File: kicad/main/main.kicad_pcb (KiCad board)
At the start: 2 copper layers, 44.5 x 35 mm, 19 parts, among them J2 Conn_01x02, J3 Conn_01x07_Pin, J4 Conn_01x04_Pin, P1 USB_C_Plug_USB2.0, SW1 MK-12C03-G015, SW3 SW_Push, SW4 SW_Push, U1 HUSB237, U2 ZX-PH2.0-WT4P

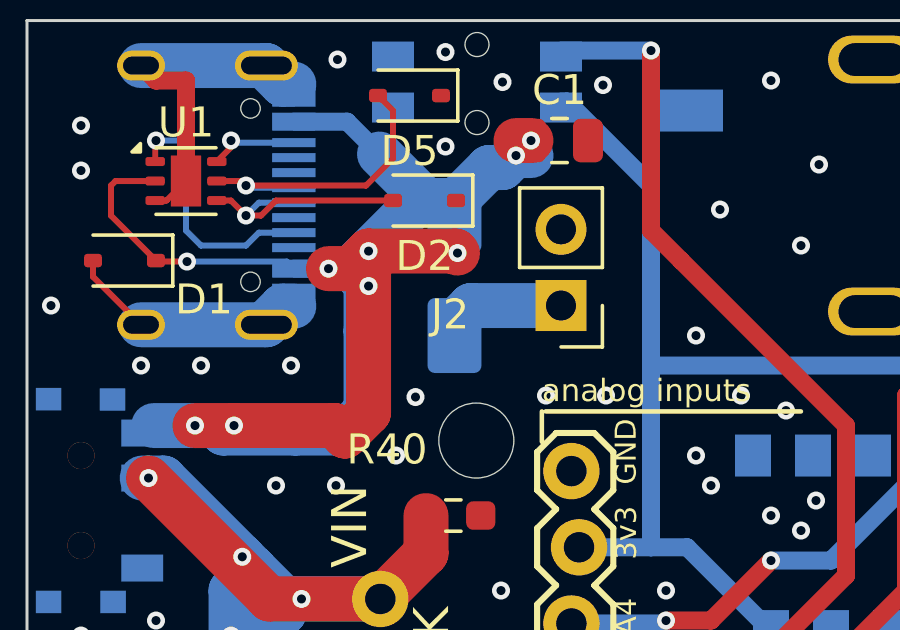
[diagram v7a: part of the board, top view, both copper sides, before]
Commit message: Increased trace widths
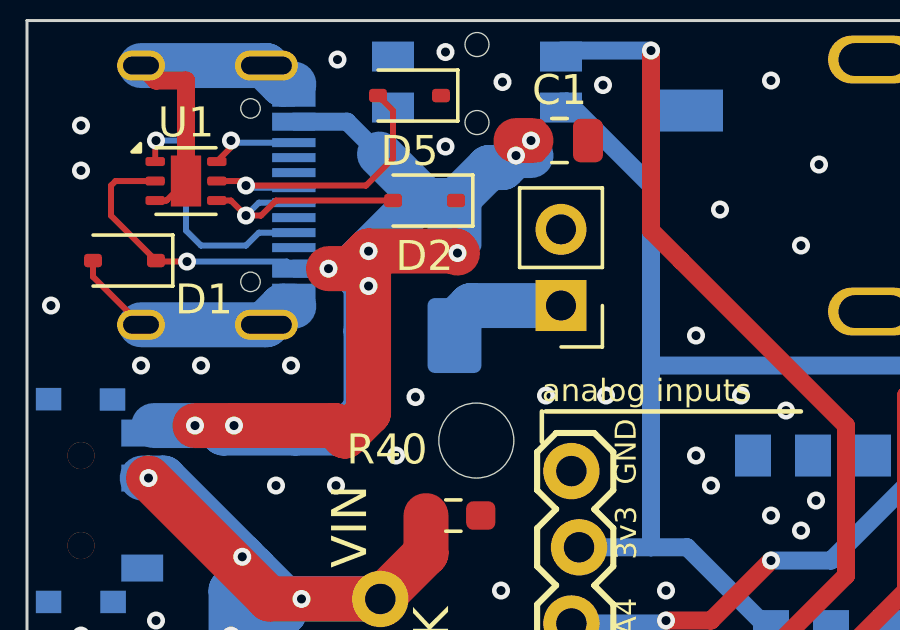
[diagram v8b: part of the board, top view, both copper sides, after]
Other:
- board text added: "BAT"
